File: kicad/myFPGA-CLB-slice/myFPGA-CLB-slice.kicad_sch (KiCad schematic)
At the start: 38 parts, among them J1 Conn_01x04, J10 Conn_01x02, J11 Conn_01x02, J12 Conn_01x04, J13 Conn_01x04, J14 Conn_01x04, J15 Conn_01x04, J2 Conn_01x04, J3 Conn_01x04, J4 Conn_01x04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

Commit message: more kicad layouts
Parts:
- gave numbers to parts that had none: 19
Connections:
- net +3V3: now also R2.2
- net GND: no longer R2.2
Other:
- moved on the sheet: R2

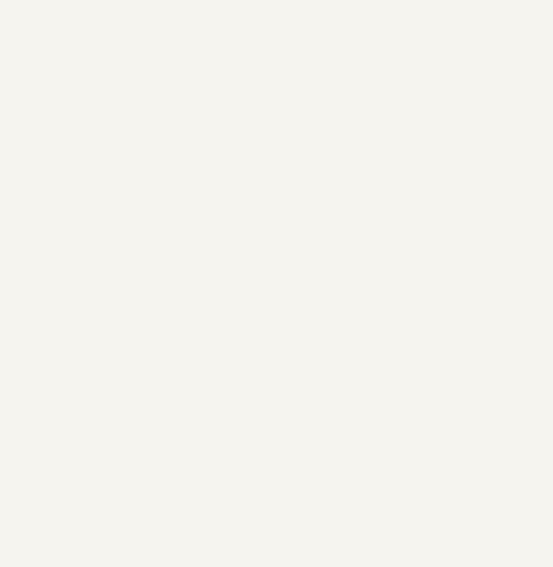
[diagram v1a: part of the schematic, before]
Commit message: CLB requires rev.2
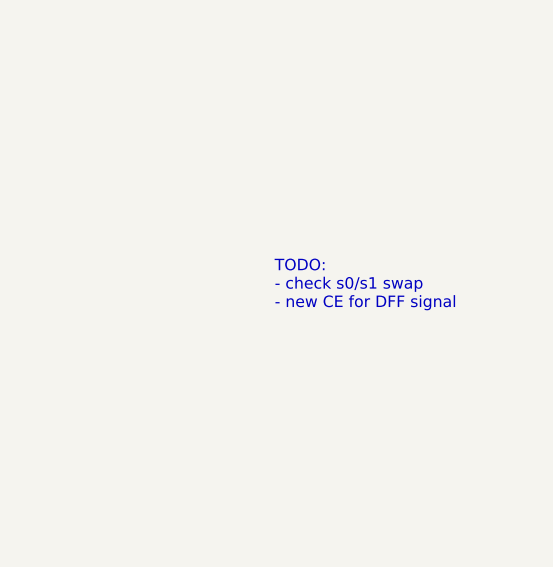
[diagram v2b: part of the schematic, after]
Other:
- note added: "TODO: - check s0/s1 swap - new CE for DFF signal"
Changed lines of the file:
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@@
+    (effects (font (size 1.27 1.27)) (justify left bottom))
+  )
+  (text "TODO:\n- check s0/s1 swap\n- new CE for DFF signal" (at 304.8 113.03 0)
     (effects (font (size 1.27 1.27)) (justify left bottom))
   )

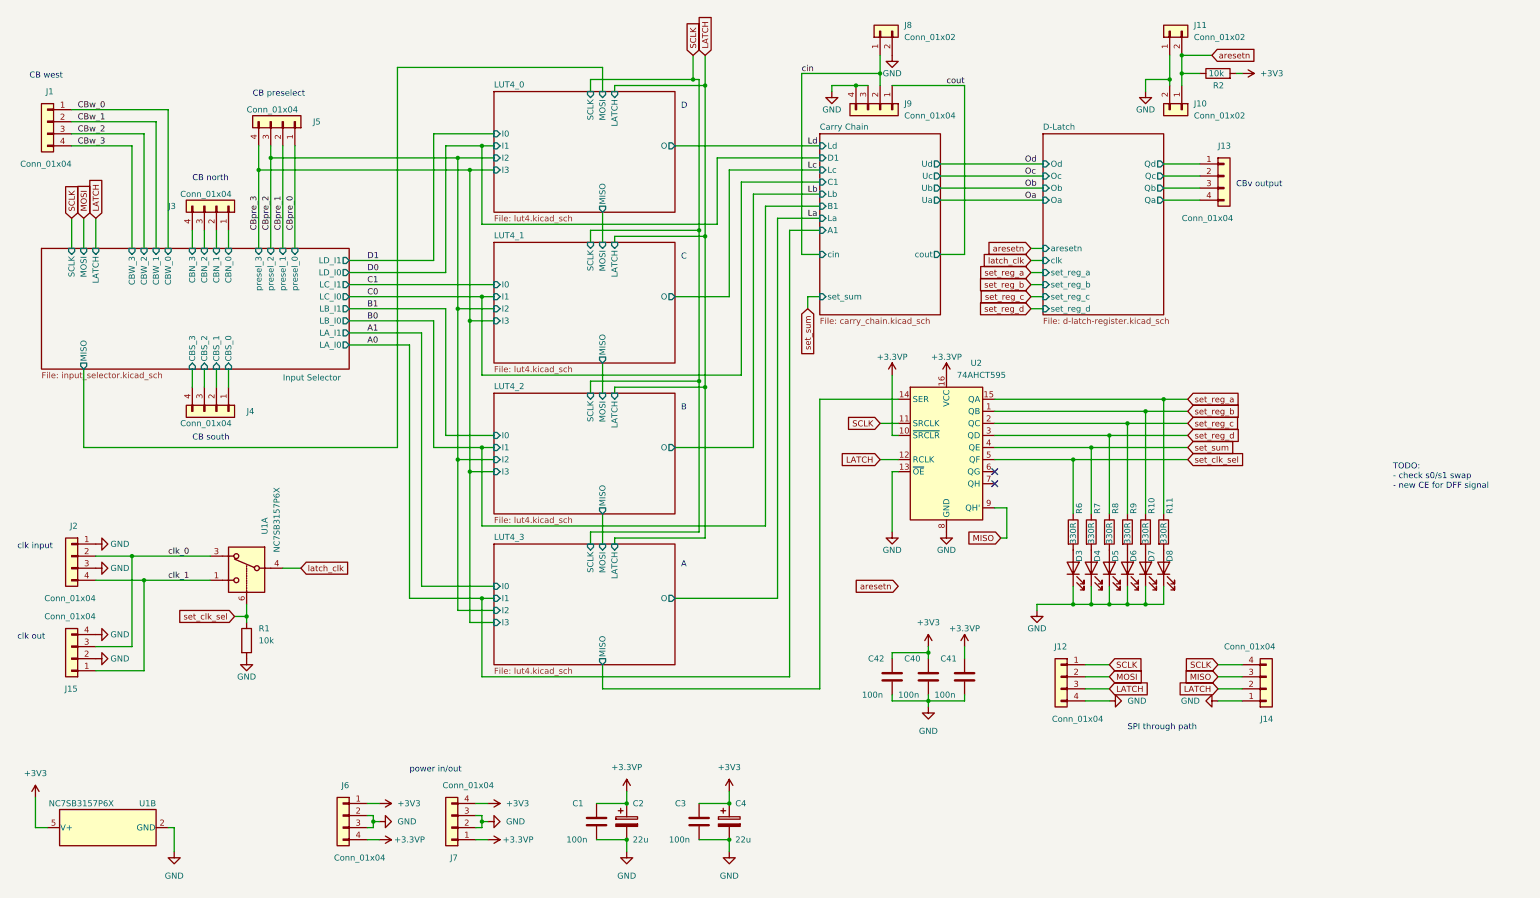
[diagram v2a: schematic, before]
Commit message: CLB slice rev. 2.0 - fix aresetn pullup instead of pulldown - new feature: clock enable - fixes S0 and S1 flipped
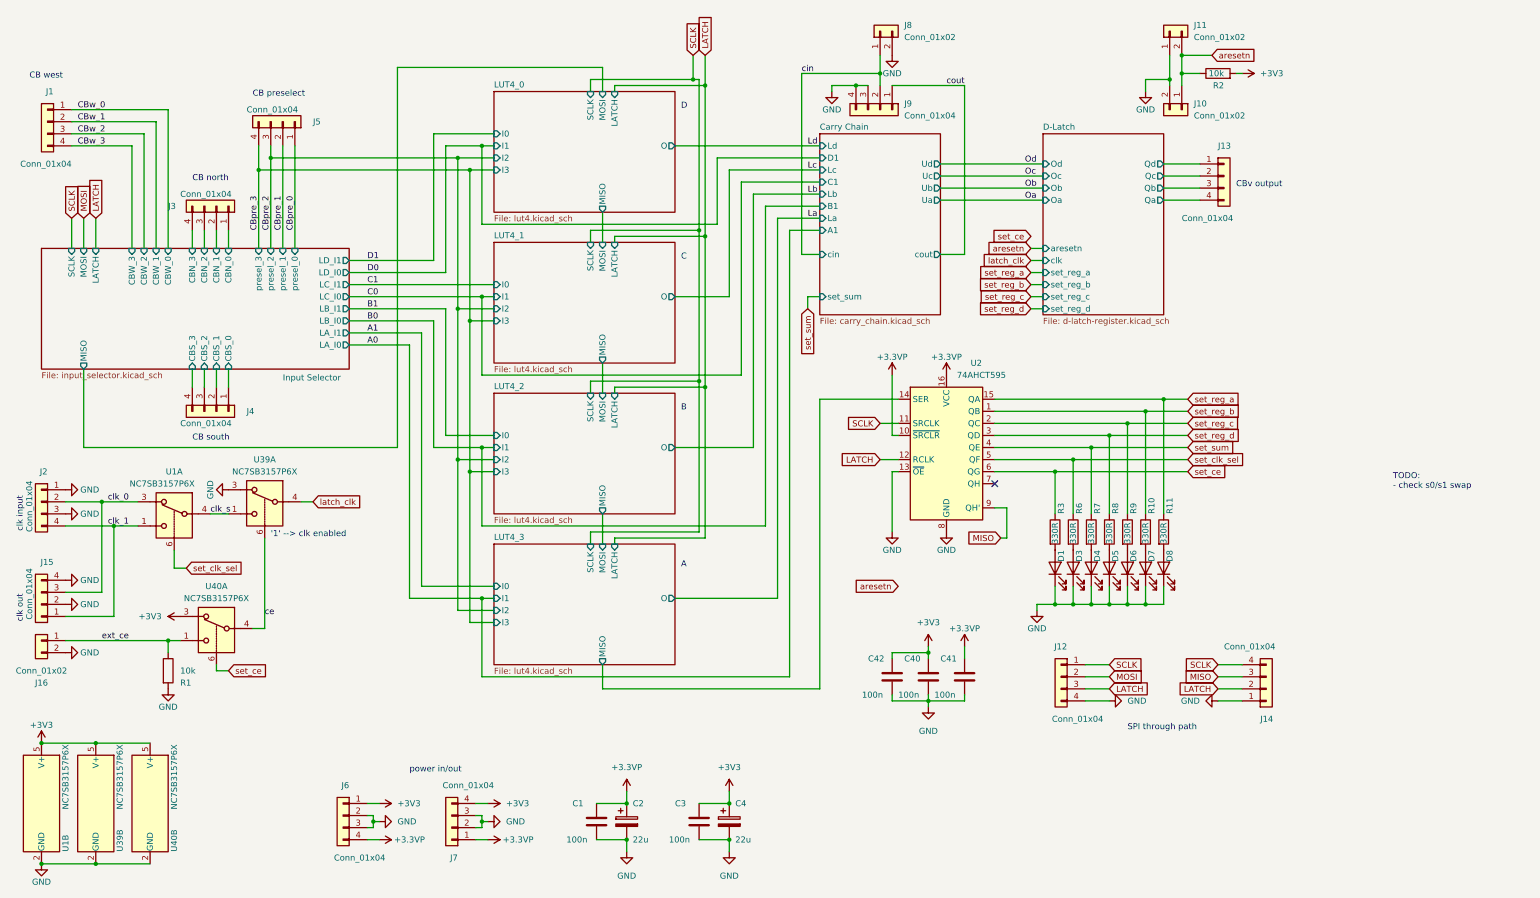
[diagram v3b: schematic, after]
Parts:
- added D1: LED (green), LED_SMD:LED_0805_2012Metric, symbol Device:LED
- added J16: Conn_01x02, Connector_PinHeader_2.54mm:PinHeader_1x02_P2.54mm_Horizontal, symbol Connector_Generic:Conn_01x02
- added R3: 330R, Resistor_SMD:R_0603_1608Metric, symbol Device:R
- added U39, U40: NC7SB3157P6X, Package_TO_SOT_SMD:SOT-363_SC-70-6, symbol Analog_Switch:NC7SB3157P6X
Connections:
- net +3V3: now also U39.5 (V+), U40.3, U40.5 (V+)
- net GND: now also D1.1 (K), J16.2 (Pin_2), U39.2 (GND), U39.3, U40.2 (GND)
- net latch_clk: now also U39.4; no longer U1.4
- net set_clk_sel: no longer R1.1
- net set_ce: now reaches U2.6 (QG)
- net set_ce: now also R3.1, U40.6
- new net: D1.2 (A), R3.2
- new net ce: U39.6, U40.4
- new net clk_s: U1.4, U39.1
- new net ext_ce: J16.1 (Pin_1), R1.1, U40.1
- no-connect marks 2 -> 1
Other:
- note added: "'1' --> clk enabled"
- note added: "TODO: - check s0/s1 swap"
- note removed: "TODO: - check s0/s1 swap - new CE for DFF signal"
- moved on the sheet: J15, J2, R1, U1A, U1B
